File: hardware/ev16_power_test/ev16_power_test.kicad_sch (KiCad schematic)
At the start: 181 parts, among them CN1 Conn_05x02_Female, CN2 PJ-242, J1 USB_C_Receptacle, J10 Conn_01x03_Pin, J11 Conn_02x05_Counter_Clockwise, J12 Conn_01x01, J13 Conn_01x01, J14 Conn_01x01, J15 Conn_01x01, J16 Conn_01x01, J17 Conn_01x01, J18 Conn_01x01, J19 Conn_01x01, J2 Conn_01x02_Socket, J20 Conn_01x01, J21 Conn_01x01, J3 AudioJack4, J4 Conn_02x03_Odd_Even, J5 Conn_02x03_Odd_Even, J6 Conn_02x05_Counter_Clockwise, J7 Conn_02x05_Counter_Clockwise, J8 Conn_02x05_Counter_Clockwise, J9 Conn_02x05_Counter_Clockwise, Q1 2N7002, Q2 2N7002, Q3 2N7002, SW1 SW_SPDT, SW2 SW_Push, SW3 SW_Push, SW4 SW_Push, SW5 SW_Push, SW6 SW_Push, SW7 SW_Push, U1 BQ21040DBV, U10 STM32F405RGTx, U12 XC6227C301MR-G, U2 USBLC6-2P6, U3 STM32F072CBTx, U4 CH340C, U5 TPS63060, U6 WM8960CGEFL/RV, U7 ESP32-S3-WROOM-1, U8 M24C02-RMN6TP, U9 TPS2116DRL, Y1 Crystal_GND24

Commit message: Completed ev16 power test board
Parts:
- CN2: JLCPCB Part # (none) -> C431536
- J12, J13, J14, J15, J16, J17, J18, J19, J20, J21: footprint Connector_PinHeader_2.54mm:PinHeader_1x01_P2.54mm_Vertical -> Connector_PinSocket_2.00mm:PinSocket_1x01_P2.00mm_Vertical; JLCPCB Part # (none) -> C2882984
- J3: JLCPCB Part # (none) -> C431535
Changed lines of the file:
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@@
 			)
 		)
-		(property "Footprint" "Connector_PinHeader_2.54mm:PinHeader_1x01_P2.54mm_Vertical"
+		(property "Footprint" "Connector_PinSocket_2.00mm:PinSocket_1x01_P2.00mm_Vertical"
 			(at 326.39 304.8 0)
 			(effects
@@
 			)
 		)
+		(property "JLCPCB Part #" "C2882984"
+			(at 326.39 304.8 0)
+			(effects
+				(font
+					(size 1.27 1.27)
+				)
+				(hide yes)
+			)
+		)
 		(pin "1"
 		)
@@
 			)
 		)
-		(property "Footprint" "Connector_PinHeader_2.54mm:PinHeader_1x01_P2.54mm_Vertical"
+		(property "Footprint" "Connector_PinSocket_2.00mm:PinSocket_1x01_P2.00mm_Vertical"
 			(at 124.46 342.9 0)
 			(effects
@@
 			)
 		)
+		(property "JLCPCB Part #" "C2882984"
+			(at 124.46 342.9 0)
+			(effects
+				(font
+					(size 1.27 1.27)
+				)
+				(hide yes)
+			)
+		)
 		(pin "1"
 		)
@@
 			)
 		)
-		(property "Footprint" "Connector_PinHeader_2.54mm:PinHeader_1x01_P2.54mm_Vertical"
+		(property "Footprint" "Connector_PinSocket_2.00mm:PinSocket_1x01_P2.00mm_Vertical"
 			(at 363.22 306.07 0)
 			(effects
@@
 			)
 		)
+		(property "JLCPCB Part #" "C2882984"
+			(at 363.22 306.07 90)
+			(effects
+				(font
+					(size 1.27 1.27)
+				)
+				(hide yes)
+			)
+		)
 		(pin "1"
 		)
@@
 			)
 		)
+		(property "JLCPCB Part #" "C431535"
+			(at 328.93 231.14 0)
+			(effects
+				(font
+					(size 1.27 1.27)
+				)
+				(hide yes)
+			)
+		)
 		(pin "S"
 		)
@@
 			)
 		)
-		(property "Footprint" "Connector_PinHeader_2.54mm:PinHeader_1x01_P2.54mm_Vertical"
+		(property "Footprint" "Connector_PinSocket_2.00mm:PinSocket_1x01_P2.00mm_Vertical"
 			(at 175.26 309.88 0)
 			(effects
@@
 			)
 		)
+		(property "JLCPCB Part #" "C2882984"
+			(at 175.26 309.88 90)
+			(effects
+				(font
+					(size 1.27 1.27)
+				)
+				(hide yes)
+			)
+		)
 		(pin "1"
 		)
@@
 			)
 		)
-		(property "Footprint" "Connector_PinHeader_2.54mm:PinHeader_1x01_P2.54mm_Vertical"
+		(property "Footprint" "Connector_PinSocket_2.00mm:PinSocket_1x01_P2.00mm_Vertical"
 			(at 354.33 306.07 0)
 			(effects
@@
 			)
 		)
+		(property "JLCPCB Part #" "C2882984"
+			(at 354.33 306.07 90)
+			(effects
+				(font
+					(size 1.27 1.27)
+				)
+				(hide yes)
+			)
+		)
 		(pin "1"
 		)
@@
 			)
 		)
-		(property "Footprint" "Connector_PinHeader_2.54mm:PinHeader_1x01_P2.54mm_Vertical"
+		(property "Footprint" "Connector_PinSocket_2.00mm:PinSocket_1x01_P2.00mm_Vertical"
 			(at 372.11 306.07 0)
 			(effects
@@
 			)
 		)
+		(property "JLCPCB Part #" "C2882984"
+			(at 372.11 306.07 90)
+			(effects
+				(font
+					(size 1.27 1.27)
+				)
+				(hide yes)
+			)
+		)
 		(pin "1"
 		)
@@
 			)
 		)
-		(property "Footprint" "Connector_PinHeader_2.54mm:PinHeader_1x01_P2.54mm_Vertical"
+		(property "Footprint" "Connector_PinSocket_2.00mm:PinSocket_1x01_P2.00mm_Vertical"
 			(at 227.33 364.49 0)
 			(effects
@@
 			)
 		)
+		(property "JLCPCB Part #" "C2882984"
+			(at 227.33 364.49 90)
+			(effects
+				(font
+					(size 1.27 1.27)
+				)
+				(hide yes)
+			)
+		)
 		(pin "1"
 		)
@@
 			)
 		)
-		(property "Footprint" "Connector_PinHeader_2.54mm:PinHeader_1x01_P2.54mm_Vertical"
+		(property "Footprint" "Connector_PinSocket_2.00mm:PinSocket_1x01_P2.00mm_Vertical"
 			(at 217.17 364.49 0)
 			(effects
@@
 			)
 		)
+		(property "JLCPCB Part #" "C2882984"
+			(at 217.17 364.49 90)
+			(effects
+				(font
+					(size 1.27 1.27)
+				)
+				(hide yes)
+			)
+		)
 		(pin "1"
 		)
@@
 			)
 		)
-		(property "Footprint" "Connector_PinHeader_2.54mm:PinHeader_1x01_P2.54mm_Vertical"
+		(property "Footprint" "Connector_PinSocket_2.00mm:PinSocket_1x01_P2.00mm_Vertical"
 			(at 165.1 309.88 0)
 			(effects
@@
 			)
 		)
+		(property "JLCPCB Part #" "C2882984"
+			(at 165.1 309.88 90)
+			(effects
+				(font
+					(size 1.27 1.27)
+				)
+				(hide yes)
+			)
+		)
 		(pin "1"
 		)
@@
 			)
 		)
-		(property "Footprint" "Connector_PinHeader_2.54mm:PinHeader_1x01_P2.54mm_Vertical"
+		(property "Footprint" "Connector_PinSocket_2.00mm:PinSocket_1x01_P2.00mm_Vertical"
 			(at 326.39 312.42 0)
 			(effects
@@
 			)
 		)
+		(property "JLCPCB Part #" "C2882984"
+			(at 326.39 312.42 0)
+			(effects
+				(font
+					(size 1.27 1.27)
+				)
+				(hide yes)
+			)
+		)
 		(pin "1"
 		)
@@
 			(at 328.93 213.36 0)
 			(effects
+				(font
+					(size 1.27 1.27)
+				)
+				(hide yes)
+			)
+		)
+		(property "JLCPCB Part #" "C431536"
+			(at 328.93 213.36 0)
+			(effects

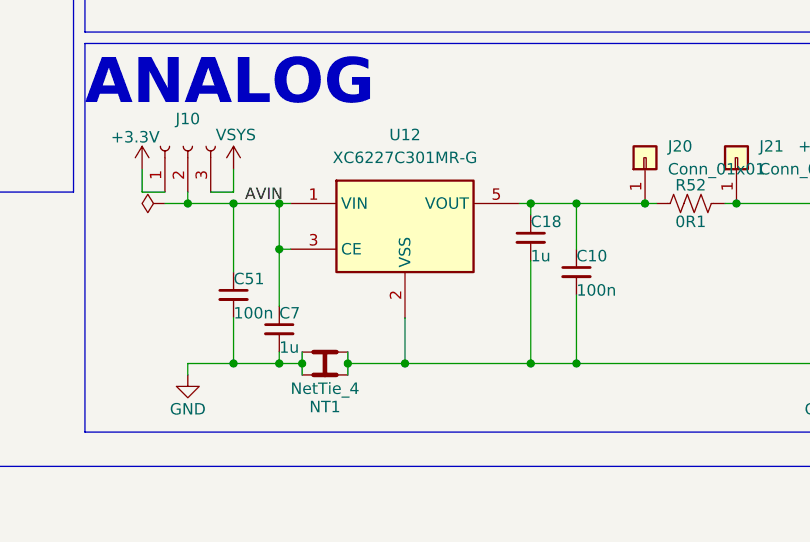
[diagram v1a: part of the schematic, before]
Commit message: Fixed rotation, added a production file for no tht parts
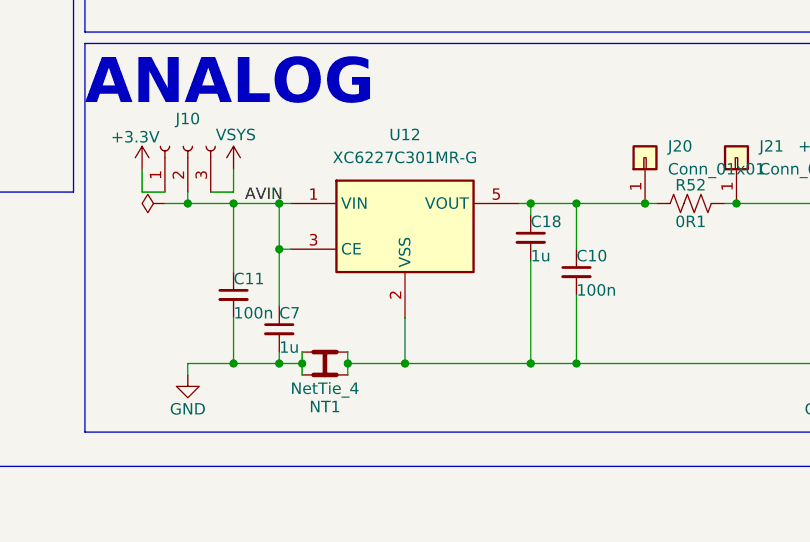
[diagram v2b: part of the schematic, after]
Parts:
- removed C51: 100n, Capacitor_SMD:C_0402_1005Metric, symbol Device:C_Small
- added C11: 100n, Capacitor_SMD:C_0805_2012Metric, symbol Device:C_Small
- C10: footprint Capacitor_SMD:C_0402_1005Metric -> Capacitor_SMD:C_0805_2012Metric
- J10, U12: FT Rotation Offset (none) -> 90
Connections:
- net AVIN: now also C11.1
- net GND: now also C11.2
